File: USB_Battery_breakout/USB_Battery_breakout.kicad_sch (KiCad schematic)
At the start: 33 parts, among them J1 USB_C_Receptacle_USB2.0_16P, J2 Conn_01x03, J3 Conn_01x06, J4 Conn_01x06, SW1 SW_Push, U1 BQ24259RGER, U2 TPS7A0533PDBV

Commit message: Prepare power module PCB
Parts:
- C1: footprint Capacitor_SMD:C_0603_1608Metric -> Capacitor_SMD:C_0402_1005Metric; JLCPCB C1622 -> (none)
- C9: footprint Capacitor_SMD:C_0603_1608Metric -> Capacitor_SMD:C_0402_1005Metric; JLCPCB C19666 -> C23733
- L1: value 1u -> 1uH
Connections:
- net 3V3: now also J3.5 (Pin_5); no longer J4.1 (Pin_1)
- net GND: now also J3.6 (Pin_6); no longer J3.1 (Pin_1)
- net PSEL: now also J3.3 (Pin_3); no longer J3.5 (Pin_5)
- net SCL: now also J4.2 (Pin_2), U1.5 (SCL); no longer J4.3 (Pin_3), U1.6 (SDA)
- net SDA: now also J4.3 (Pin_3), U1.6 (SDA); no longer J4.2 (Pin_2), U1.5 (SCL)
- net SYS: now also R2.1, R3.1; no longer D2.2 (A), D3.2 (A)
- net VBAT: now also J3.4 (Pin_4); no longer J3.6 (Pin_6)
- net VBUS: now also J4.1 (Pin_1); no longer J3.4 (Pin_4)
- net at D2.1 (K): now also U1.4 (STAT); no longer R2.1
- net at R2.2: now also D2.2 (A); no longer U1.4 (STAT)
- net at D3.1 (K): now also U1.3 (~{PG}); no longer R3.1
- net at R3.2: now also D3.2 (A); no longer U1.3 (~{PG})
- net D_MINUS renamed D-
- net D_PLUS renamed D+
- net D+: now also J3.1 (Pin_1); no longer J3.3 (Pin_3)
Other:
- moved on the sheet: D2, D3, R2, R3

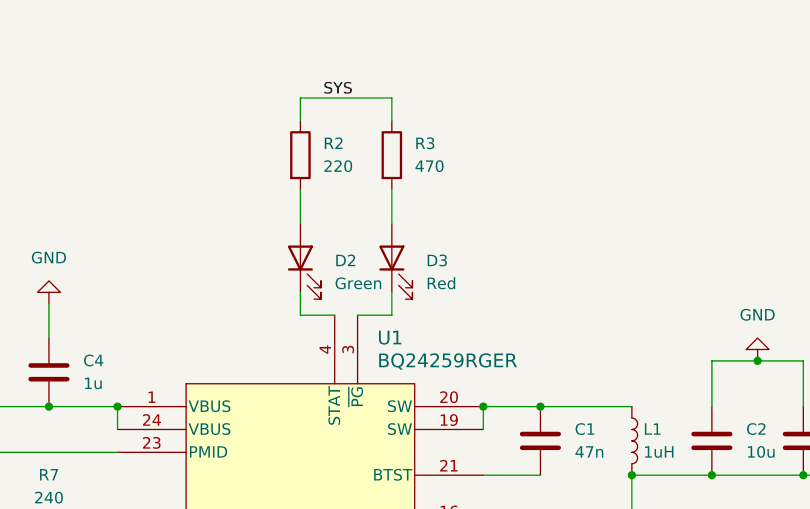
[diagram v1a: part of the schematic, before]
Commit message: Make PG LED green, STAT red
STAT is usually an error, PG is normal operation.
Added JLCPCB part numbers for more components.
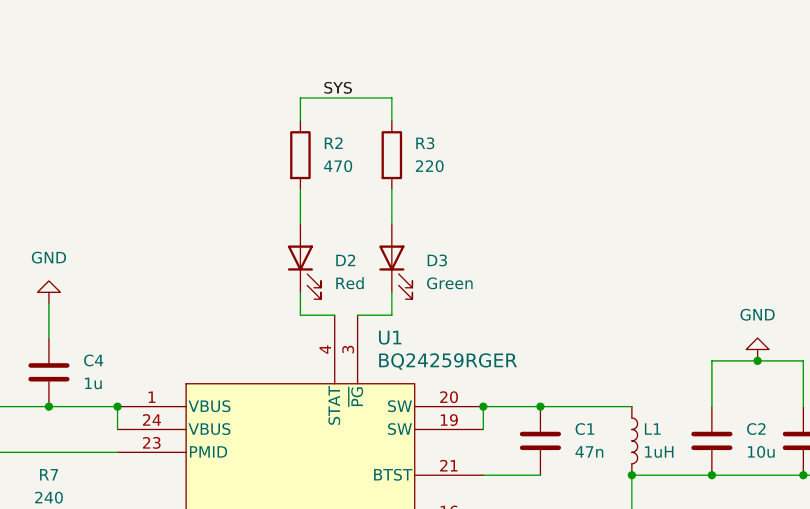
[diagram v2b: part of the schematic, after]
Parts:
- C1: JLCPCB (none) -> C5142571
- D2: value Green -> Red; JLCPCB C72043 -> C2286
- D3: value Red -> Green; JLCPCB C2286 -> C72043
- J1: JLCPCB (none) -> C3025063
- L1: JLCPCB (none) -> C161082
- R2: value 220 -> 470; JLCPCB C25091 -> C25117
- R3: value 470 -> 220; JLCPCB C25117 -> C25091
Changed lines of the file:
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@@
 			)
 		)
-		(property "Value" "220"
+		(property "Value" "470"
 			(at 160.02 53.3399 0)
 			(effects
@@
 			)
 		)
-		(property "JLCPCB" "C25091"
+		(property "JLCPCB" "C25117"
 			(at 157.48 52.07 0)
 			(effects
@@
 			)
 		)
+		(property "JLCPCB" "C161082"
+			(at 194.31 83.82 0)
+			(effects
+				(font
+					(size 1.27 1.27)
+				)
+				(hide yes)
+			)
+		)
 		(pin "1"
 		)
@@
 			)
 		)
+		(property "JLCPCB" "C3025063"
+			(at 41.91 95.25 0)
+			(effects
+				(font
+					(size 1.27 1.27)
+				)
+				(hide yes)
+			)
+		)
 		(pin "B12"
 		)
@@
 			)
 		)
-		(property "Value" "Red"
+		(property "Value" "Green"
 			(at 171.45 66.3574 90)
 			(effects
@@
 			)
 		)
-		(property "JLCPCB" "C2286"
+		(property "JLCPCB" "C72043"
 			(at 167.64 63.5 90)
 			(effects
@@
 			)
 		)
-		(property "Value" "Green"
+		(property "Value" "Red"
 			(at 161.29 66.3574 90)
 			(effects
@@
 			)
 		)
-		(property "JLCPCB" "C72043"
+		(property "JLCPCB" "C2286"
 			(at 157.48 63.5 90)
 			(effects
@@
 			)
 		)
-		(property "Value" "470"
+		(property "Value" "220"
 			(at 170.18 53.3399 0)
 			(effects
@@
 			)
 		)
-		(property "JLCPCB" "C25117"
+		(property "JLCPCB" "C25091"
 			(at 167.64 52.07 0)
 			(effects
@@
 			)
 		)
-		(property "JLCPCB" ""
+		(property "JLCPCB" "C5142571"
 			(at 184.15 83.82 0)
 			(effects

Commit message: Update USB-C connector ID
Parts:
- J1: JLCPCB C3025063 -> C165948
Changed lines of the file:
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@@
 			)
 		)
-		(property "JLCPCB" "C3025063"
+		(property "JLCPCB" "C165948"
 			(at 41.91 95.25 0)
 			(effects
